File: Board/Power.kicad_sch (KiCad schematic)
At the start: 89 parts, among them J2 DCJ0202, Q4 IRLML5203

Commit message: work on r1.3
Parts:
- removed C151: 47u, cbm_ultipet_v1:E2,5-6, symbol cbm_ultipet_v1-eagle-import:CPOL-EUE2.5-6
- removed J2: DCJ0202, cbm_ultipet_v1:DCJ0202, symbol cbm_ultipet_v1-eagle-import:DCJ0202
- removed Q4: IRLML5203, cbm_ultipet_v1:MICRO3, symbol cbm_ultipet_v1-eagle-import:IRLML5203
- removed R48: 100k, cbm_ultipet_v1:0207_2V, symbol cbm_ultipet_v1-eagle-import:R-EU_0207/2V
- added C151, C156: 47u, cbm_ultipet_v1:E2,5-6, symbol micropet_v3-eagle-import:CPOL-EUE5-6
- added J2: USB_C_Receptacle_USB2.0_14P, Connector_USB:USB_C_Receptacle_GCT_USB4085, symbol Connector:USB_C_Receptacle_USB2.0_14P
- added R41, R42: 5k1, cbm_ultipet_v1:0207_2V, symbol micropet_v3-eagle-import:R-EU_0207/2V
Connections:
- net GND: now also C151.-, C156.-, J2.A1 (GND), J2.A12 (GND), J2.B1 (GND), J2.B12 (GND), J2.S1 (SHIELD), R41.1, R42.1
- net VCC: now also C151.+, C156.+, J2.A4 (VBUS), J2.A9 (VBUS), J2.B4 (VBUS), J2.B9 (VBUS)
- new net: J2.A5 (CC1), R42.2
- new net: J2.B5 (CC2), R41.2
- new net UCD+: J2.A6 (D+), J2.B6 (D+)
- new net UCD-: J2.A7 (D-), J2.B7 (D-)
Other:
- note added: "1.1A: - change footprint of power switch to a combined one 1.2A: - add LED connector - add 3.3V for I/O 1.3A: - USB-C power connector"
- note added: "CBM-ULTIPET-V1.3A"
- note added: "CSA-ULTIPET-V1.3A-20250806"
- note removed: "1.1A: - change footprint of power switch to a combined one 1.2A: - add LED connector - add 3.3V for I/O"
- note removed: "CBM-ULTIPET-V1.2A"
- note removed: "CSA-ULTIPET-V1.2A-20241010"
- moved on the sheet: JP8, SW1

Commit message: more layout work on r1.3
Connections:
- net VCC: no longer C151.+, C156.+, J2.A4 (VBUS), J2.A9 (VBUS), J2.B4 (VBUS), J2.B9 (VBUS)
- net VCCIN: now also C151.+, C156.+, J2.A4 (VBUS), J2.A9 (VBUS), J2.B4 (VBUS), J2.B9 (VBUS)
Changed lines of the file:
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@@
 	(wire
 		(pts
+			(xy 82.55 25.4) (xy 82.55 33.02)
+		)
+		(stroke
+			(width 0)
+			(type default)
+		)
+	)
+	(wire
+		(pts
 			(xy 132.08 96.52) (xy 132.08 93.98)
 		)
@@
 	(wire
 		(pts
+			(xy 85.09 25.4) (xy 82.55 25.4)
+		)
+		(stroke
+			(width 0)
+			(type default)
+		)
+	)
+	(wire
+		(pts
 			(xy 97.79 45.72) (xy 97.79 39.37)
 		)
@@
 	(wire
 		(pts
-			(xy 82.55 27.94) (xy 82.55 33.02)
-		)
-		(stroke
-			(width 0)
-			(type default)
-		)
-	)
-	(wire
-		(pts
 			(xy 106.68 187.96) (xy 114.3 187.96)
 		)
@@
 		)
 	)
+	(global_label "VCCIN"
+		(shape input)
+		(at 85.09 25.4 0)
+		(fields_autoplaced yes)
+		(effects
+			(font
+				(size 1.27 1.27)
+			)
+			(justify left)
+		)
+		(property "Intersheetrefs" "${INTERSHEET_REFS}"
+			(at 93.6391 25.4 0)
+			(effects
+				(font
+					(size 1.27 1.27)
+				)
+				(justify left)
+				(hide yes)
+			)
+		)
+	)
 	(global_label "V12"
 		(shape bidirectional)
@@
 					(unit 1)
 				)
-			)
-		)
-	)
-	(symbol
-		(lib_id "micropet_v3-eagle-import:VCC")
-		(at 82.55 25.4 0)
-		(unit 1)
-		(exclude_from_sim no)
-		(in_bom yes)
-		(on_board yes)
-		(dnp no)
-		(property "Reference" "#V049"
-			(at 82.55 25.4 0)
-			(effects
-				(font
-					(size 1.27 1.27)
-				)
-				(hide yes)
-			)
-		)
-		(property "Value" "VCC"
-			(at 80.645 22.225 0)
-			(effects
-				(font
-					(size 1.778 1.5113)
-				)
-				(justify left bottom)
-			)
-		)
-		(property "Footprint" ""
-			(at 82.55 25.4 0)
-			(effects
-				(font
-					(size 1.27 1.27)
-				)
-				(hide yes)
-			)
-		)
-		(property "Datasheet" ""
-			(at 82.55 25.4 0)
-			(effects
-				(font
-					(size 1.27 1.27)
-				)
-				(hide yes)
-			)
-		)
-		(property "Description" ""
-			(at 82.55 25.4 0)
-			(effects
-				(font
-					(size 1.27 1.27)
-				)
-				(hide yes)
-			)
-		)
-		(pin "1"
-		)
-		(instances
-			(project "cbm_ultipet_v1"
-				(path "/4dd2dd78-173f-4b46-8cce-4ed940435c94/f2a7836e-baa5-4eed-9e59-e26d91b4d1a6"
-					(reference "#V049")
-					(unit 1)
-				)

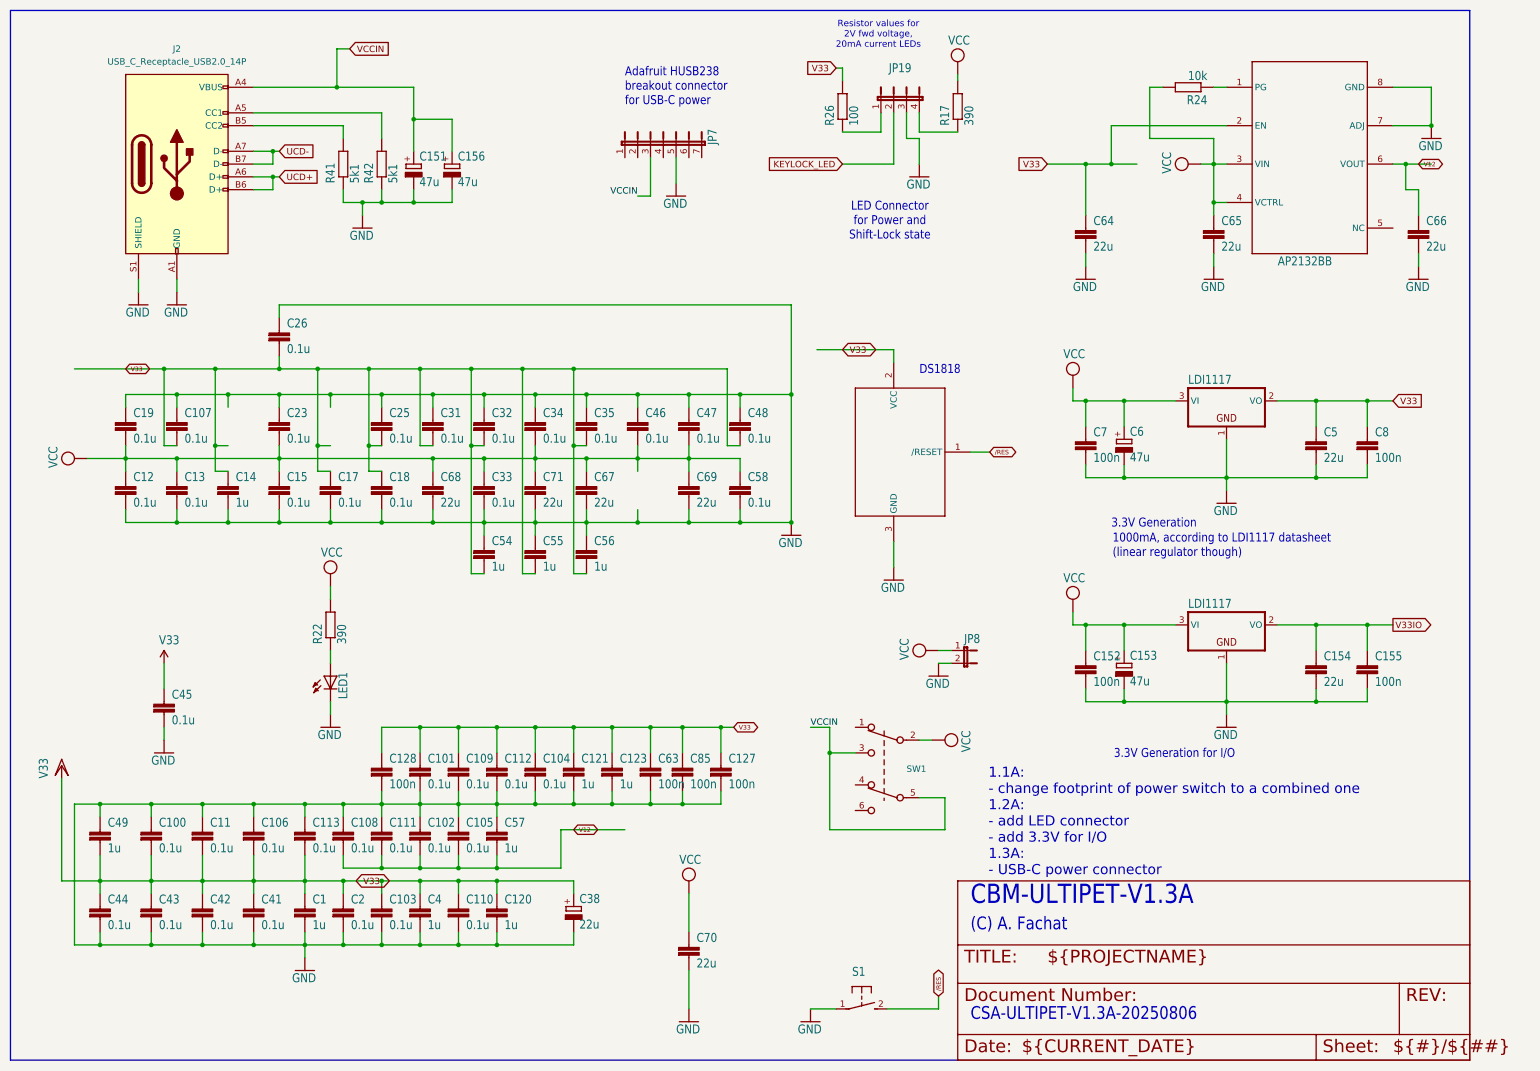
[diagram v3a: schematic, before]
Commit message: fix DS1818 layout
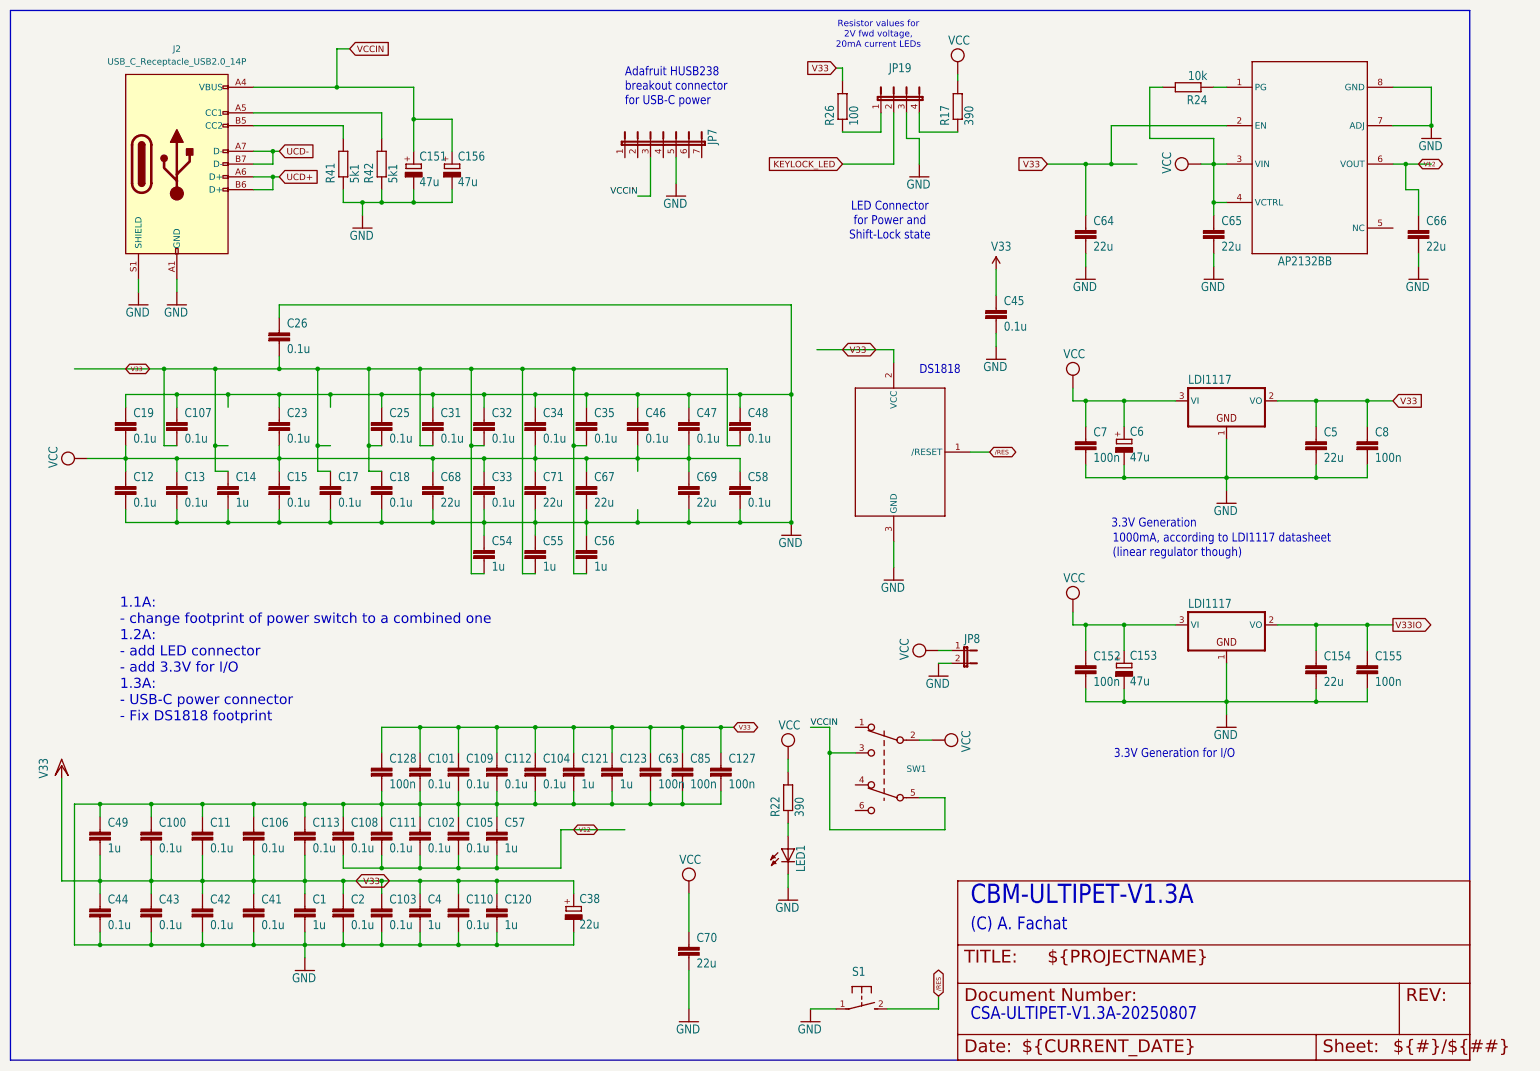
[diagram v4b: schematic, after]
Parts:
- DS1818: footprint cbm_ultipet_v1:TO92 -> Package_TO_SOT_THT:TO-92_Inline
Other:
- note added: "1.1A: - change footprint of power switch to a combined one 1.2A: - add LED connector - add 3.3V for I/O 1.3A: - USB-C power connector - Fix DS1818 footprint"
- note added: "CSA-ULTIPET-V1.3A-20250807"
- note removed: "1.1A: - change footprint of power switch to a combined one 1.2A: - add LED connector - add 3.3V for I/O 1.3A: - USB-C power connector"
- note removed: "CSA-ULTIPET-V1.3A-20250806"
- moved on the sheet: C45, LED1, R22
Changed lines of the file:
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@@
 		)
 	)
-	(text "1.1A:\n- change footprint of power switch to a combined one\n1.2A:\n- add LED connector\n- add 3.3V for I/O\n1.3A:\n- USB-C power connector"
+	(text "1.1A:\n- change footprint of power switch to a combined one\n1.2A:\n- add LED connector\n- add 3.3V for I/O\n1.3A:\n- USB-C power connector\n- Fix DS1818 footprint"
 		(exclude_from_sim no)
-		(at 211.836 178.816 0)
+		(at 39.497 146.685 0)
 		(effects
 			(font
@@
 		)
 	)
-	(text "CSA-ULTIPET-V1.3A-20250806"
+	(text "CSA-ULTIPET-V1.3A-20250807"
 		(exclude_from_sim no)
 		(at 208.28 218.44 0)
@@
 	(wire
 		(pts
-			(xy 81.28 157.48) (xy 81.28 154.94)
+			(xy 172.085 191.77) (xy 172.085 189.23)
 		)
 		(stroke
@@
 	(wire
 		(pts
-			(xy 81.28 134.62) (xy 81.28 132.08)
+			(xy 172.085 168.91) (xy 172.085 166.37)
 		)
 		(stroke
@@
 	(wire
 		(pts
-			(xy 81.28 147.32) (xy 81.28 144.78)
+			(xy 172.085 181.61) (xy 172.085 179.07)
 		)
 		(stroke
@@
 	(wire
 		(pts
-			(xy 48.26 152.4) (xy 48.26 147.32)
+			(xy 213.36 74.295) (xy 213.36 69.215)
 		)
 		(stroke
@@
 	(wire
 		(pts
-			(xy 48.26 162.56) (xy 48.26 160.02)
+			(xy 213.36 84.455) (xy 213.36 81.915)
 		)
 		(stroke
@@
 	(symbol
 		(lib_id "cbm_ultipet_v1-eagle-import:GND")
-		(at 48.26 165.1 0)
+		(at 213.36 86.995 0)
 		(unit 1)
 		(exclude_from_sim no)
@@
 		(dnp no)
 		(property "Reference" "#GND028"
-			(at 48.26 165.1 0)
+			(at 213.36 86.995 0)
 			(effects
 				(font
@@
 		)
 		(property "Value" "GND"
-			(at 45.72 167.64 0)
+			(at 210.82 89.535 0)
 			(effects
 				(font
@@
 		)
 		(property "Footprint" ""
-			(at 48.26 165.1 0)
+			(at 213.36 86.995 0)
 			(effects
 				(font
@@
 		)
 		(property "Datasheet" ""
-			(at 48.26 165.1 0)
+			(at 213.36 86.995 0)
 			(effects
 				(font
@@
 		)
 		(property "Description" ""
-			(at 48.26 165.1 0)
+			(at 213.36 86.995 0)
 			(effects
 				(font
@@
 	(symbol
 		(lib_id "cbm_ultipet_v1-eagle-import:GND")
-		(at 81.28 160.02 0)
+		(at 172.085 194.31 0)
 		(unit 1)
 		(exclude_from_sim no)
@@
 		(dnp no)
 		(property "Reference" "#GND042"
-			(at 81.28 160.02 0)
+			(at 172.085 194.31 0)
 			(effects
 				(font
@@
 		)
 		(property "Value" "GND"
-			(at 78.74 162.56 0)
+			(at 169.545 196.85 0)
 			(effects
 				(font
@@
 		)
 		(property "Footprint" ""
-			(at 81.28 160.02 0)
+			(at 172.085 194.31 0)
 			(effects
 				(font
@@
 		)
 		(property "Datasheet" ""
-			(at 81.28 160.02 0)
+			(at 172.085 194.31 0)
 			(effects
 				(font
@@
 		)
 		(property "Description" ""
-			(at 81.28 160.02 0)
+			(at 172.085 194.31 0)
 			(effects
 				(font
@@
 	(symbol
 		(lib_id "cbm_ultipet_v1-eagle-import:R-EU_0207/2V")
-		(at 81.28 139.7 90)
+		(at 172.085 173.99 90)
 		(unit 1)
 		(exclude_from_sim no)
@@
 		(dnp no)
 		(property "Reference" "R22"
-			(at 79.7814 143.51 0)
+			(at 170.5864 177.8 0)
 			(effects
 				(font
@@
 		)
 		(property "Value" "390"
-			(at 84.582 143.51 0)
+			(at 175.387 177.8 0)
 			(effects
 				(font
@@
 		)
 		(property "Footprint" "cbm_ultipet_v1:0207_2V"
-			(at 81.28 139.7 0)
+			(at 172.085 173.99 0)
 			(effects
 				(font
@@
 		)
 		(property "Datasheet" ""
-			(at 81.28 139.7 0)
+			(at 172.085 173.99 0)
 			(effects
 				(font
@@
 		)
 		(property "Description" ""
-			(at 81.28 139.7 0)
+			(at 172.085 173.99 0)
 			(effects
 				(font
@@
 	(symbol
 		(lib_id "cbm_ultipet_v1-eagle-import:3.3V")
-		(at 48.26 147.32 0)
+		(at 213.36 69.215 0)
 		(unit 1)
 		(exclude_from_sim no)
@@
 		(dnp no)
 		(property "Reference" "#V033"
-			(at 48.26 147.32 0)
+			(at 213.36 69.215 0)
 			(effects
 				(font
@@
 		)
 		(property "Value" "V33"
-			(at 47.244 143.764 0)
+			(at 212.344 65.659 0)
 			(effects
 				(font
@@
 		)
 		(property "Footprint" ""
-			(at 48.26 147.32 0)
+			(at 213.36 69.215 0)
 			(effects
 				(font
@@
 		)
 		(property "Datasheet" ""
-			(at 48.26 147.32 0)
+			(at 213.36 69.215 0)
 			(effects
 				(font
@@
 		)
 		(property "Description" ""
-			(at 48.26 147.32 0)
+			(at 213.36 69.215 0)
 			(effects
 				(font
@@
 	(symbol
 		(lib_id "cbm_ultipet_v1-eagle-import:VCC")
-		(at 81.28 129.54 0)
+		(at 172.085 163.83 0)
 		(unit 1)
 		(exclude_from_sim no)
@@
 		(dnp no)
 		(property "Reference" "#V021"
-			(at 81.28 129.54 0)
+			(at 172.085 163.83 0)
 			(effects
 				(font
@@
 		)
 		(property "Value" "VCC"
-			(at 79.375 126.365 0)
+			(at 170.18 160.655 0)
 			(effects
 				(font
@@
 		)
 		(property "Footprint" ""
-			(at 81.28 129.54 0)
+			(at 172.085 163.83 0)
 			(effects
 				(font
@@
 		)
 		(property "Datasheet" ""
-			(at 81.28 129.54 0)
+			(at 172.085 163.83 0)
 			(effects
 				(font
@@
 		)
 		(property "Description" ""
-			(at 81.28 129.54 0)
+			(at 172.085 163.83 0)
 			(effects
 				(font
@@
 	(symbol
 		(lib_id "cbm_ultipet_v1-eagle-import:C-EUC0603")
-		(at 48.26 154.94 0)
+		(at 213.36 76.835 0)
 		(unit 1)
 		(exclude_from_sim no)
@@
 		(dnp no)
 		(property "Reference" "C45"
-			(at 49.784 154.559 0)
+			(at 214.884 76.454 0)
 			(effects
 				(font
@@
 		)
 		(property "Value" "0.1u"
-			(at 49.784 159.639 0)
+			(at 214.884 81.534 0)
 			(effects
 				(font
@@
 		)
 		(property "Footprint" "cbm_ultipet_v1:C0603"
-			(at 48.26 154.94 0)
+			(at 213.36 76.835 0)
 			(effects
 				(font
@@
 		)
 		(property "Datasheet" ""
-			(at 48.26 154.94 0)
+			(at 213.36 76.835 0)
 			(effects
 				(font
@@
 		)
 		(property "Description" ""
-			(at 48.26 154.94 0)
+			(at 213.36 76.835 0)
 			(effects
 				(font
@@
 			)
 		)
-		(property "Footprint" "cbm_ultipet_v1:TO92"
+		(property "Footprint" "Package_TO_SOT_THT:TO-92_Inline"
 			(at 190.5 102.87 0)
 			(effects
@@
 	(symbol
 		(lib_id "cbm_ultipet_v1-eagle-import:LED3MM")
-		(at 81.28 149.86 0)
+		(at 172.085 184.15 0)
 		(unit 1)
 		(exclude_from_sim no)
@@
 		(dnp no)
 		(property "Reference" "LED1"
-			(at 84.836 154.432 90)
+			(at 175.641 188.722 90)
 			(effects
 				(font
@@
 		)
 		(property "Value" "LED3MM"
-			(at 86.995 154.432 90)
+			(at 177.8 188.722 90)
 			(effects
 				(font
@@
 		)
 		(property "Footprint" "cbm_ultipet_v1:LED3MM"
-			(at 81.28 149.86 0)
+			(at 172.085 184.15 0)
 			(effects
 				(font
@@
 		)
 		(property "Datasheet" ""
-			(at 81.28 149.86 0)
+			(at 172.085 184.15 0)
 			(effects
 				(font
@@
 		)
 		(property "Description" ""
-			(at 81.28 149.86 0)
+			(at 172.085 184.15 0)
 			(effects
 				(font

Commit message: new USB C conn; BOM work
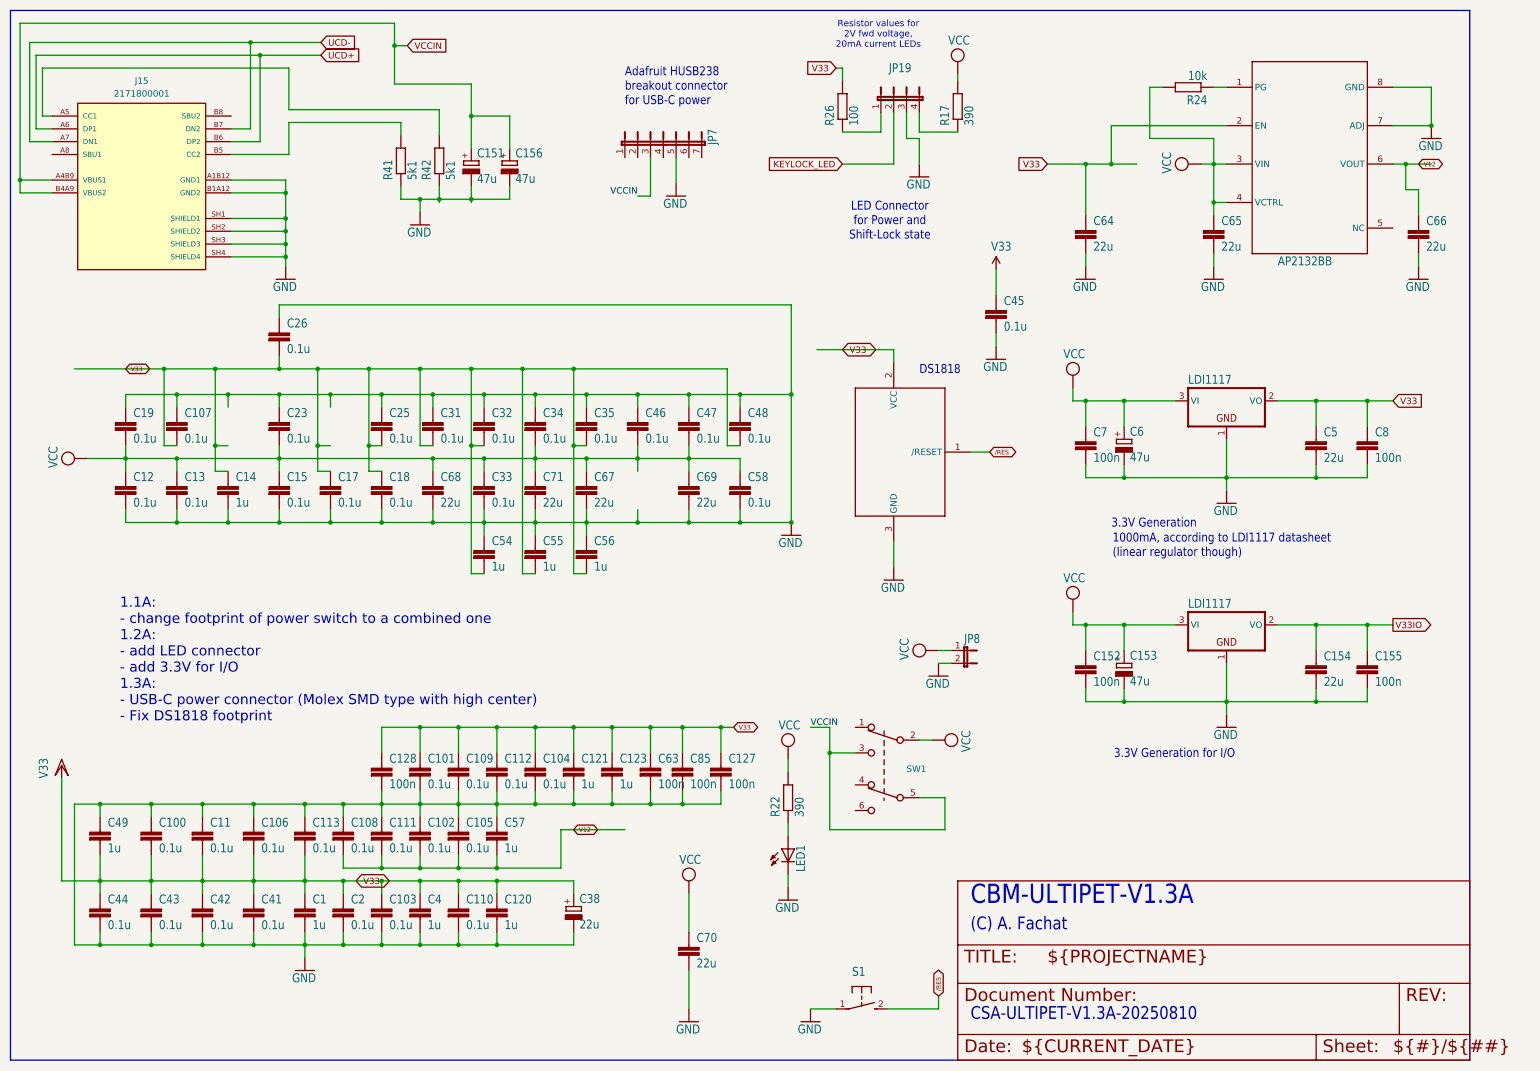
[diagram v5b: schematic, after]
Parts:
- removed J2: USB_C_Receptacle_USB2.0_14P, Connector_USB:USB_C_Receptacle_GCT_USB4085, symbol Connector:USB_C_Receptacle_USB2.0_14P
- added J15: 2171800001, cbm_ultipet_v1:MOLEX_2171800001, symbol Symbols:2171800001
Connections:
- net GND: now also J15.A1B12 (GND1), J15.B1A12 (GND2), J15.SH1 (SHIELD1), J15.SH2 (SHIELD2), J15.SH3 (SHIELD3), J15.SH4 (SHIELD4)
- net UCD+: now also J15.A6 (DP1), J15.B6 (DP2)
- net UCD-: now also J15.A7 (DN1), J15.B7 (DN2)
- net VCCIN: now also J15.A4B9 (VBUS1), J15.B4A9 (VBUS2)
- net at R42.2: now also J15.A5 (CC1)
- net at R41.2: now also J15.B5 (CC2)
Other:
- note added: "1.1A: - change footprint of power switch to a combined one 1.2A: - add LED connector - add 3.3V for I/O 1.3A: - USB-C power connector (Molex SMD type with high center) - Fix DS1818 footprint"
- note added: "CSA-ULTIPET-V1.3A-20250810"
- note removed: "1.1A: - change footprint of power switch to a combined one 1.2A: - add LED connector - add 3.3V for I/O 1.3A: - USB-C power connector - Fix DS1818 footprint"
- note removed: "CSA-ULTIPET-V1.3A-20250807"
- moved on the sheet: C151, C156, R41, R42
